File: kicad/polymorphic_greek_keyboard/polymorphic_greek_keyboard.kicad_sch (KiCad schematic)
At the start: 0 parts

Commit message: [ADD] an esp 32 chip to the kicad model as a means of checking the status of the imported library
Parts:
- added U1: ESP32-S2-WROVER, RF_Module:ESP32-S2-WROVER, symbol RF_Module:ESP32-S2-WROVER
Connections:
- new net: U1.1 (GND), U1.26 (GND), U1.42 (GND), U1.43 (GND)
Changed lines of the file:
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@@
 	(generator_version "9.0")
 	(paper "A4")
+	(symbol
+		(lib_id "RF_Module:ESP32-S2-WROVER")
+		(at 49.53 66.04 0)
+		(unit 1)
+		(exclude_from_sim no)
+		(in_bom yes)
+		(on_board yes)
+		(dnp no)
+		(fields_autoplaced yes)
+		(property "Reference" "U1"
+			(at 51.6733 33.02 0)
+			(effects
+				(font
+					(size 1.27 1.27)
+				)
+				(justify left)
+			)
+		)
+		(property "Value" "ESP32-S2-WROVER"
+			(at 51.6733 35.56 0)
+			(effects
+				(font
+					(size 1.27 1.27)
+				)
+				(justify left)
+			)
+		)
+		(property "Footprint" "RF_Module:ESP32-S2-WROVER"
+			(at 68.58 95.25 0)
+			(effects
+				(font
+					(size 1.27 1.27)
+				)
+				(hide yes)
+			)
+		)
+		(property "Datasheet" "https://www.espressif.com/sites/default/files/documentation/esp32-s2-wroom_esp32-s2-wroom-i_datasheet_en.pdf"
+			(at 41.91 86.36 0)
+			(effects
+				(font
+					(size 1.27 1.27)
+				)
+				(hide yes)
+			)
+		)
+		(property "Description" "RF Module, ESP32-D0WDQ6 SoC, Wi-Fi 802.11b/g/n, 32-bit, 2.7-3.6V, onboard antenna, SMD"
+			(at 49.53 66.04 0)
+			(effects
+				(font
+					(size 1.27 1.27)
+				)
+				(hide yes)
+			)
+		)
+		(pin "18"
+		)
+		(pin "33"
+		)
+		(pin "31"
+		)
+		(pin "37"
+		)
+		(pin "9"
+		)
+		(pin "14"
+		)
+		(pin "16"
+		)
+		(pin "23"
+		)
+		(pin "29"
+		)
+		(pin "36"
+		)
+		(pin "34"
+		)
+		(pin "8"
+		)
+		(pin "22"
+		)
+		(pin "6"
+		)
+		(pin "5"
+		)
+		(pin "4"
+		)
+		(pin "15"
+		)
+		(pin "35"
+		)
+		(pin "27"
+		)
+		(pin "25"
+		)
+		(pin "26"
+		)
+		(pin "11"
+		)
+		(pin "38"
+		)
+		(pin "40"
+		)
+		(pin "39"
+		)
+		(pin "2"
+		)
+		(pin "21"
+		)
+		(pin "30"
+		)
+		(pin "10"
+		)
+		(pin "42"
+		)
+		(pin "28"
+		)
+		(pin "43"
+		)
+		(pin "24"
+		)
+		(pin "1"
+		)
+		(pin "12"
+		)
+		(pin "41"
+		)
+		(pin "3"
+		)
+		(pin "7"
+		)
+		(pin "20"
+		)
+		(pin "32"
+		)
+		(pin "13"
+		)
+		(pin "17"
+		)
+		(pin "19"
+		)
+		(instances
+			(project ""
+				(path "/29d1f4c4-2c66-4ff7-ad76-620f460314f7"
+					(reference "U1")
+					(unit 1)
+				)
+			)
+		)
+	)
 	(sheet_instances
 		(path "/"

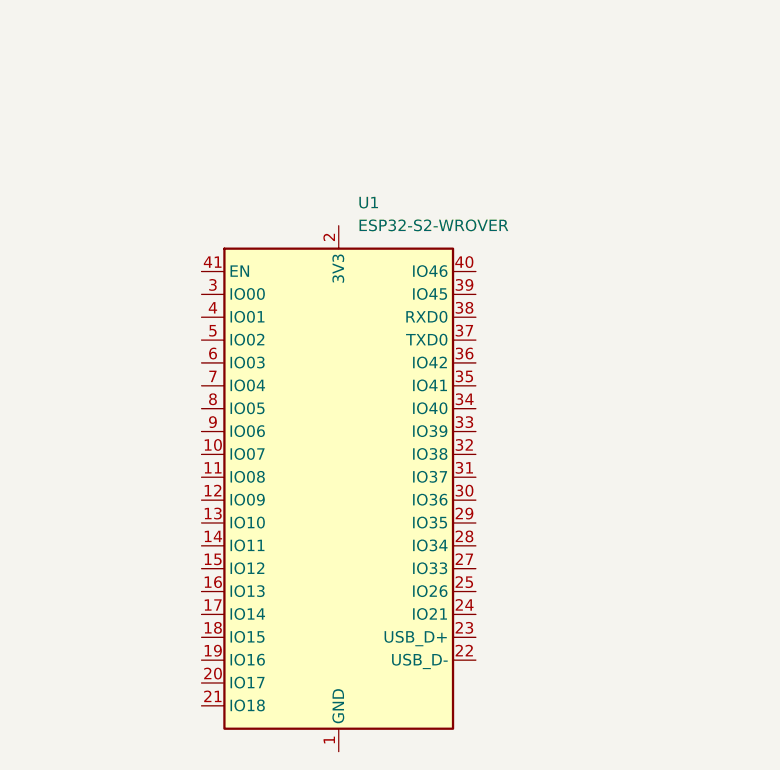
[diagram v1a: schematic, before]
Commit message: [ADD] child components requied to build the keyboard in subschema's desings in kicad
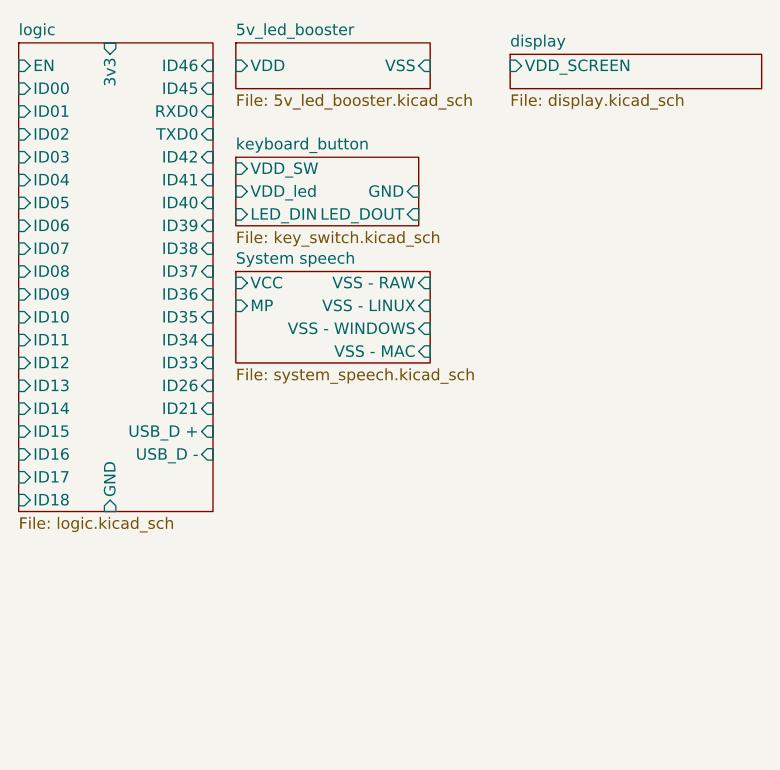
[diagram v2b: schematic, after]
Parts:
- removed U1: ESP32-S2-WROVER, RF_Module:ESP32-S2-WROVER, symbol RF_Module:ESP32-S2-WROVER
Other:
- added sheet 5v_led_booster (5v_led_booster.kicad_sch)
- added sheet System speech (system_speech.kicad_sch)
- added sheet display (display.kicad_sch)
- added sheet keyboard_button (key_switch.kicad_sch)
- added sheet logic (logic.kicad_sch)
- company: (none) -> None
- title: (none) -> Keyboard matrix
